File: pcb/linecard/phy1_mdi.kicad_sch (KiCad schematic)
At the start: 99 parts, among them J5 LPJG47036AWNL, J9 LPJG47036AWNL, U35 VSC8512, U36 ESD224DQAR, U37 ESD224DQAR, U38 ESD224DQAR, U39 ESD224DQAR, U40 ESD224DQAR, U41 ESD224DQAR, U42 ESD224DQAR, U43 ESD224DQAR, U44 ESD224DQAR, U45 ESD224DQAR, U46 ESD224DQAR, U47 ESD224DQAR, U48 ESD224DQAR, U49 ESD224DQAR, U50 ESD224DQAR, U51 ESD224DQAR, U52 ESD224DQAR, U53 ESD224DQAR, U54 ESD224DQAR, U55 ESD224DQAR, U56 ESD224DQAR, U57 ESD224DQAR, U58 ESD224DQAR, U59 ESD224DQAR

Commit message: Finished initial schematic review
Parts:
- J5, J9: footprint (none) -> azonenberg_pcb:CONN_LINKPP_LPJG47036AWNL
- U36, U37, U38, U39, U40, U41, U42, U43, U44, U45, U46, U47, U48, U49, U50, U51, U52, U53, U54, U55, U56, U57, U58, U59: footprint (none) -> azonenberg_pcb:DFN_10_0.5MM_2.5x1MM_TI_DQA
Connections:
- net CHGND: now also J9.SHLD, J9.SHLD, J9.SHLD, J9.SHLD, J9.SHLD, J9.SHLD, J9.SHLD, J9.SHLD; no longer J9.A0 (SHLD), J9.B0 (SHLD), J9.C0 (SHLD), J9.D0 (SHLD), J9.E0 (SHLD), J9.F0 (SHLD), J9.G0 (SHLD), J9.H0 (SHLD)
- net PHY0_D1_P: now also U36.6 (IO4_S); no longer U36.5 (IO4_S)
- net PHY0_D3_P: now also U37.6 (IO4_S); no longer U37.5 (IO4_S)
- net PHY10_D1_P: now also U56.6 (IO4_S); no longer U56.5 (IO4_S)
- net PHY10_D3_P: now also U57.6 (IO4_S); no longer U57.5 (IO4_S)
- net PHY11_D1_P: now also U58.6 (IO4_S); no longer U58.5 (IO4_S)
- net PHY11_D3_P: now also U59.6 (IO4_S); no longer U59.5 (IO4_S)
- net PHY1_D1_P: now also U38.6 (IO4_S); no longer U38.5 (IO4_S)
- net PHY1_D3_P: now also U39.6 (IO4_S); no longer U39.5 (IO4_S)
- net PHY2_D1_P: now also U40.6 (IO4_S); no longer U40.5 (IO4_S)
- net PHY2_D3_P: now also U41.6 (IO4_S); no longer U41.5 (IO4_S)
- net PHY3_D1_P: now also U42.6 (IO4_S); no longer U42.5 (IO4_S)
- net PHY3_D3_P: now also U43.6 (IO4_S); no longer U43.5 (IO4_S)
- net PHY4_D1_P: now also U44.6 (IO4_S); no longer U44.5 (IO4_S)
- net PHY4_D3_P: now also U45.6 (IO4_S); no longer U45.5 (IO4_S)
- net PHY5_D1_P: now also U46.6 (IO4_S); no longer U46.5 (IO4_S)
- net PHY5_D3_P: now also U47.6 (IO4_S); no longer U47.5 (IO4_S)
- net PHY6_D1_P: now also U48.6 (IO4_S); no longer U48.5 (IO4_S)
- net PHY6_D3_P: now also U49.6 (IO4_S); no longer U49.5 (IO4_S)
- net PHY7_D1_P: now also U50.6 (IO4_S); no longer U50.5 (IO4_S)
- net PHY7_D3_P: now also U51.6 (IO4_S); no longer U51.5 (IO4_S)
- net PHY8_D1_P: now also U52.6 (IO4_S); no longer U52.5 (IO4_S)
- net PHY8_D3_P: now also U53.6 (IO4_S); no longer U53.5 (IO4_S)
- net PHY9_D1_P: now also U54.6 (IO4_S); no longer U54.5 (IO4_S)
- net PHY9_D3_P: now also U55.6 (IO4_S); no longer U55.5 (IO4_S)

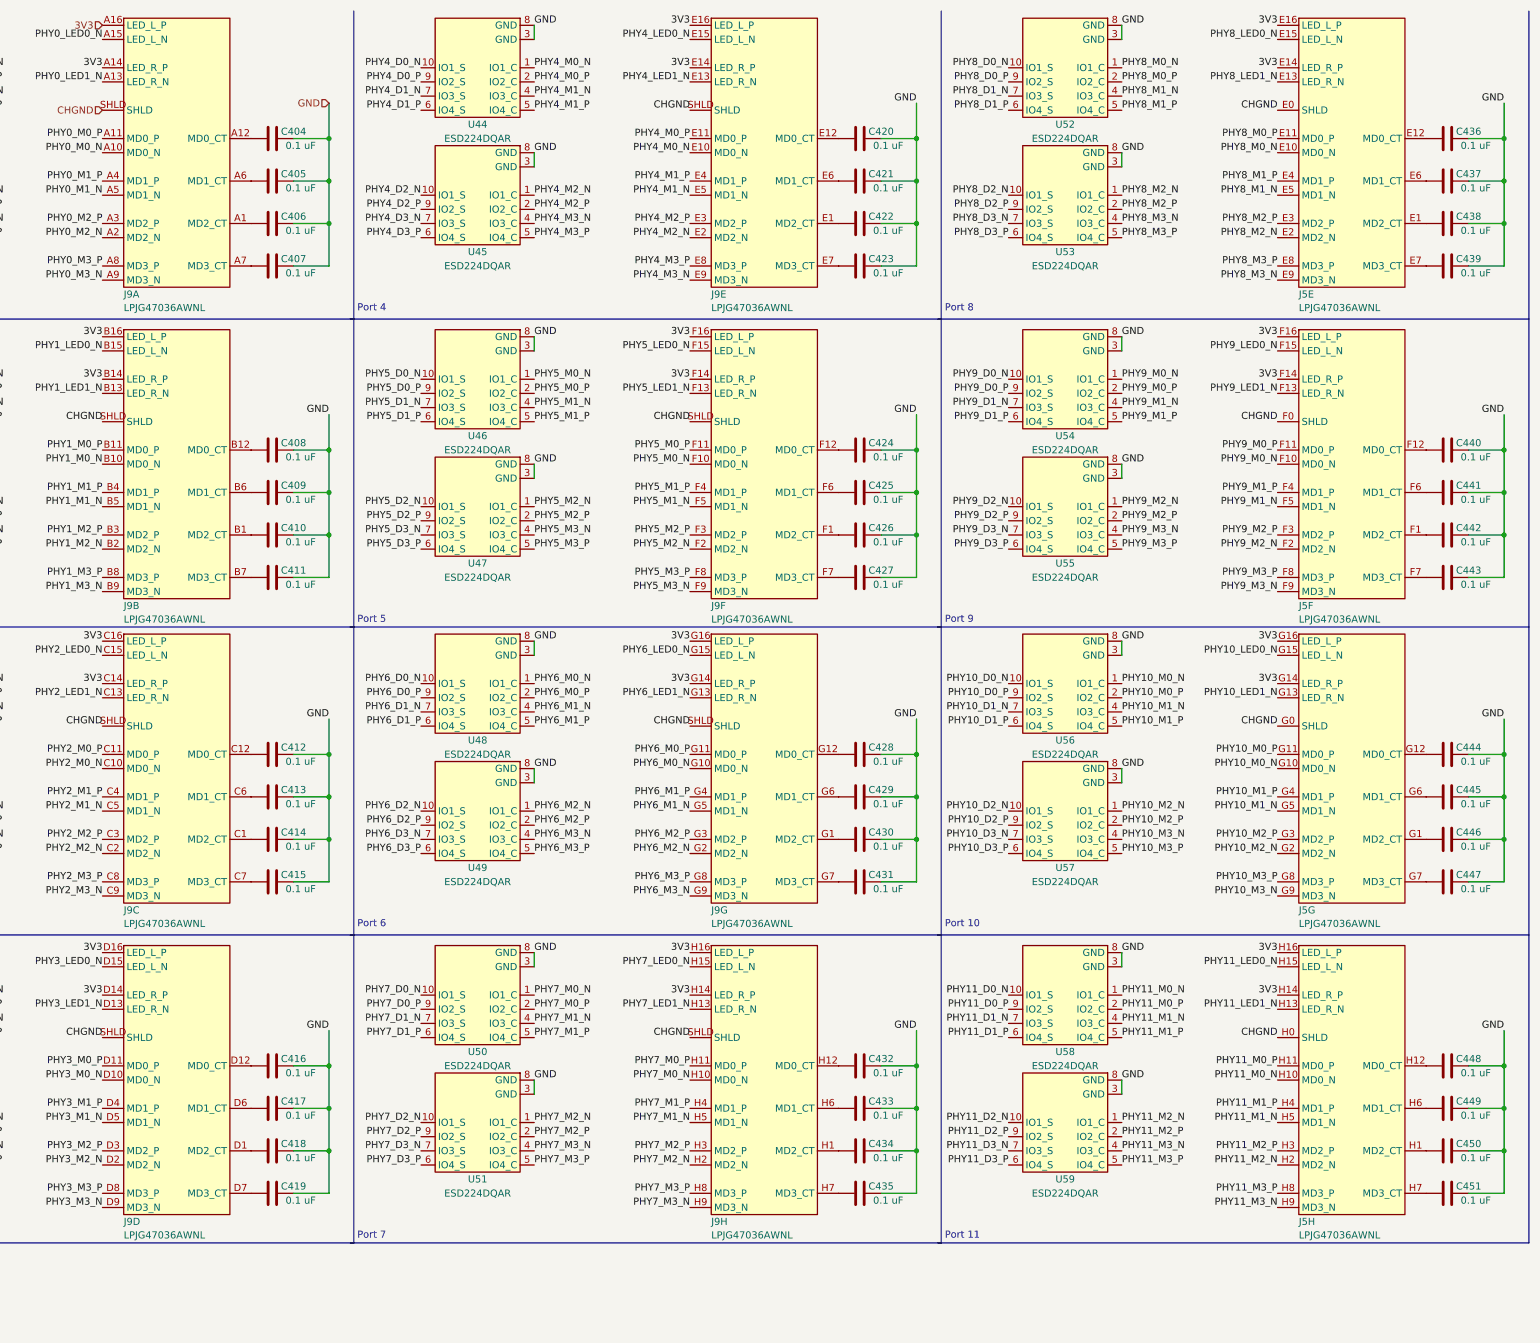
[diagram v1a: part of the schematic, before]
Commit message: COntinued routing baseT pairs on left PHY
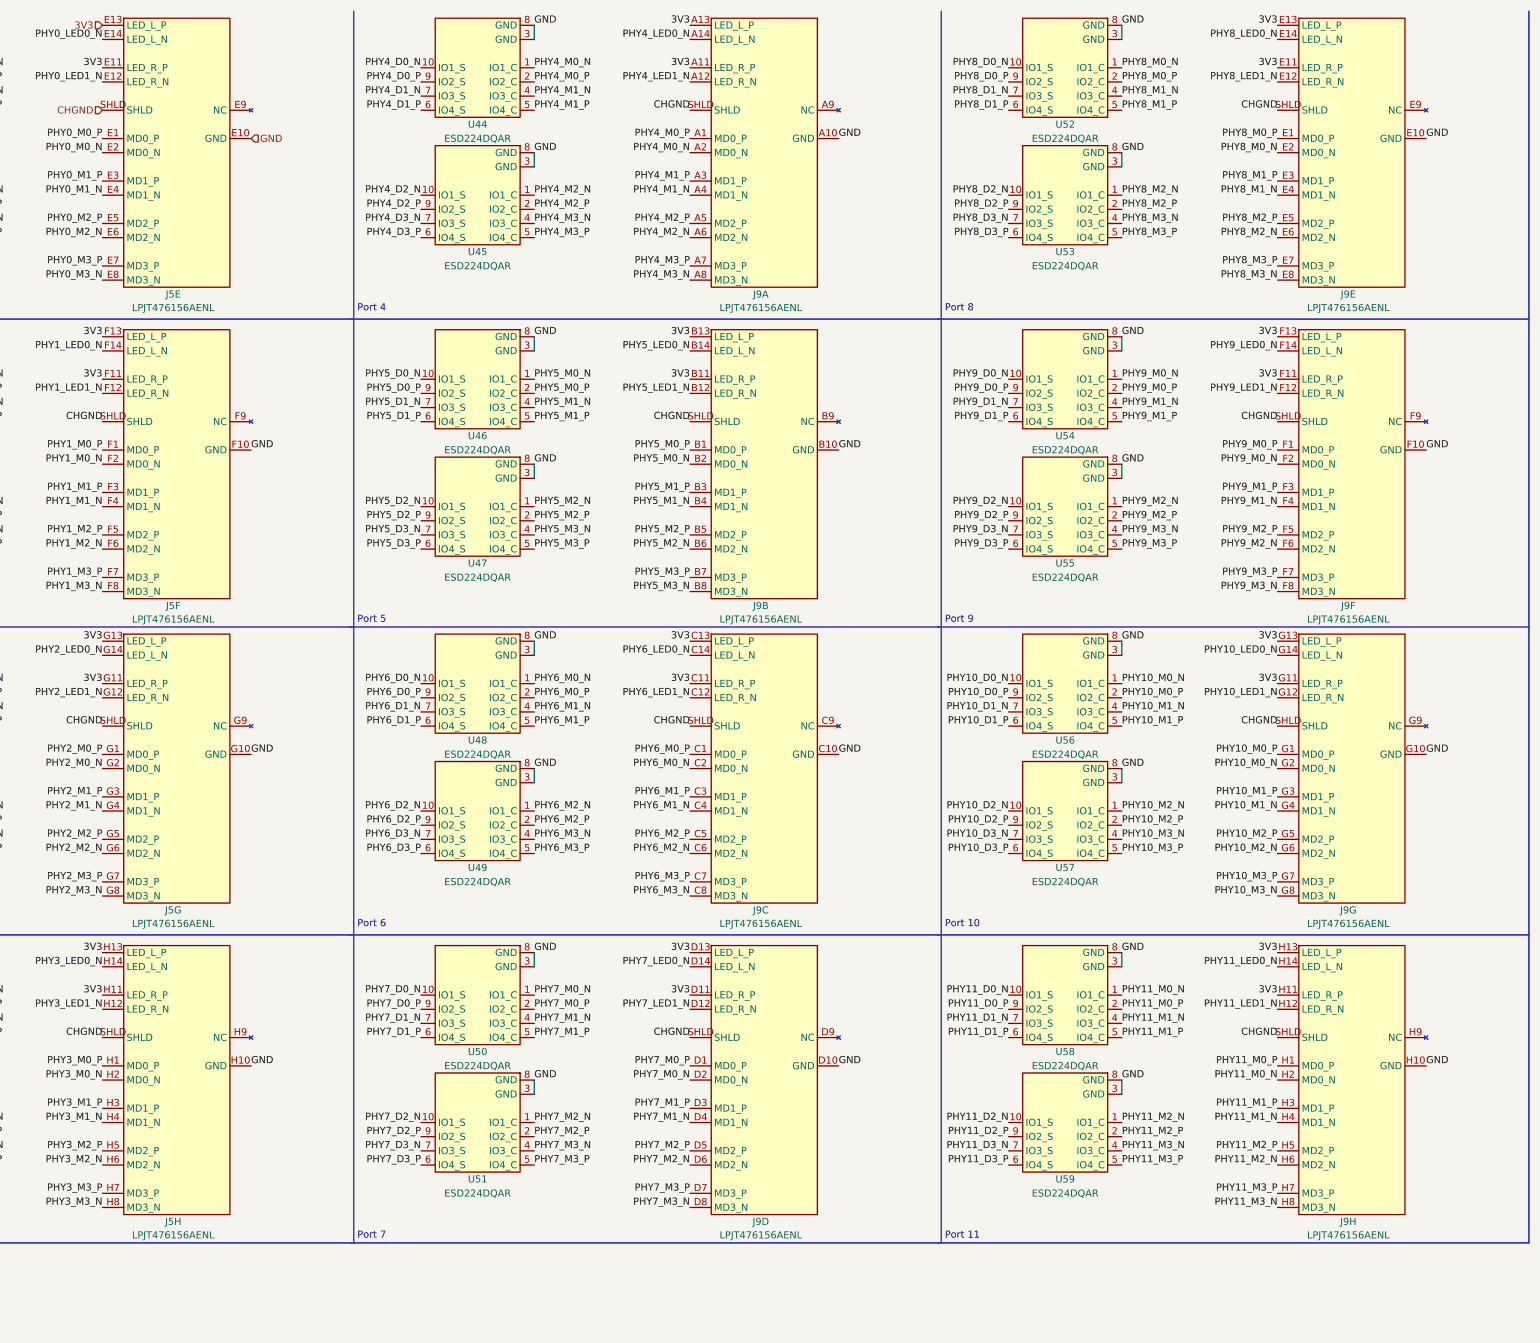
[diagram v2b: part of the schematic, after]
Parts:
- removed C404, C405, C406, C407, C408, C409, C410, C411, C412, C413, C414, C415, C416, C417, C418, C419, C420, C421, C422, C423, C424, C425, C426, C427, C428, C429, C430, C431, C432, C433, C434, C435, C436, C437, C438, C439, C440, C441, C442, C443, C444, C445, C446, C447, C448, C449, C450, C451: 0.1 uF, azonenberg_pcb:EIA_0402_CAP_NOSILK, symbol device:C
- removed J5, J9: LPJG47036AWNL, azonenberg_pcb:CONN_LINKPP_LPJG47036AWNL, symbol special-azonenberg:LPJG47036AWNL
- added J5, J9: LPJT476156AENL, azonenberg_pcb:CONN_LINKPP_LPJT476156AENL, symbol special-azonenberg:LPJT476156AENL
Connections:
- net 3V3: now also J5.E11 (LED_R_P), J5.E13 (LED_L_P), J5.F11 (LED_R_P), J5.F13 (LED_L_P), J5.G11 (LED_R_P), J5.G13 (LED_L_P), J5.H11 (LED_R_P), J5.H13 (LED_L_P), J9.A11 (LED_R_P), J9.A13 (LED_L_P), J9.B11 (LED_R_P), J9.B13 (LED_L_P), J9.C11 (LED_R_P), J9.C13 (LED_L_P), J9.D11 (LED_R_P), J9.D13 (LED_L_P), J9.E11 (LED_R_P), J9.E13 (LED_L_P), J9.F11 (LED_R_P), J9.F13 (LED_L_P), J9.G11 (LED_R_P), J9.G13 (LED_L_P), J9.H11 (LED_R_P), J9.H13 (LED_L_P)
- net CHGND: now also J5.SHLD, J5.SHLD, J5.SHLD, J5.SHLD, J9.SHLD, J9.SHLD, J9.SHLD, J9.SHLD, J9.SHLD, J9.SHLD, J9.SHLD, J9.SHLD
- net GND: now also J5.E10 (GND), J5.F10 (GND), J5.G10 (GND), J5.H10 (GND), J9.A10 (GND), J9.B10 (GND), J9.C10 (GND), J9.D10 (GND), J9.E10 (GND), J9.F10 (GND), J9.G10 (GND), J9.H10 (GND)
- net PHY0_LED0_N: now also J5.E14 (LED_L_N)
- net PHY0_LED1_N: now also J5.E12 (LED_R_N)
- net PHY0_M0_N: now also J5.E2 (MD0_N)
- net PHY0_M0_P: now also J5.E1 (MD0_P)
- net PHY0_M1_N: now also J5.E4 (MD1_N)
- net PHY0_M1_P: now also J5.E3 (MD1_P)
- net PHY0_M2_N: now also J5.E6 (MD2_N)
- net PHY0_M2_P: now also J5.E5 (MD2_P)
- net PHY0_M3_N: now also J5.E8 (MD3_N)
- net PHY0_M3_P: now also J5.E7 (MD3_P)
- net PHY10_LED0_N: now also J9.G14 (LED_L_N)
- net PHY10_LED1_N: now also J9.G12 (LED_R_N)
- net PHY10_M0_N: now also J9.G2 (MD0_N)
- net PHY10_M0_P: now also J9.G1 (MD0_P)
- net PHY10_M1_N: now also J9.G4 (MD1_N)
- net PHY10_M1_P: now also J9.G3 (MD1_P)
- net PHY10_M2_N: now also J9.G6 (MD2_N)
- net PHY10_M2_P: now also J9.G5 (MD2_P)
- net PHY10_M3_N: now also J9.G8 (MD3_N)
- net PHY10_M3_P: now also J9.G7 (MD3_P)
- net PHY11_LED0_N: now also J9.H14 (LED_L_N)
- net PHY11_LED1_N: now also J9.H12 (LED_R_N)
- net PHY11_M0_N: now also J9.H2 (MD0_N)
- net PHY11_M0_P: now also J9.H1 (MD0_P)
- net PHY11_M1_N: now also J9.H4 (MD1_N)
- net PHY11_M1_P: now also J9.H3 (MD1_P)
- net PHY11_M2_N: now also J9.H6 (MD2_N)
- net PHY11_M2_P: now also J9.H5 (MD2_P)
- net PHY11_M3_N: now also J9.H8 (MD3_N)
- net PHY11_M3_P: now also J9.H7 (MD3_P)
- net PHY1_LED0_N: now also J5.F14 (LED_L_N)
- net PHY1_LED1_N: now also J5.F12 (LED_R_N)
- net PHY1_M0_N: now also J5.F2 (MD0_N)
- net PHY1_M0_P: now also J5.F1 (MD0_P)
- net PHY1_M1_N: now also J5.F4 (MD1_N)
- net PHY1_M1_P: now also J5.F3 (MD1_P)
- net PHY1_M2_N: now also J5.F6 (MD2_N)
- net PHY1_M2_P: now also J5.F5 (MD2_P)
- net PHY1_M3_N: now also J5.F8 (MD3_N)
- net PHY1_M3_P: now also J5.F7 (MD3_P)
- net PHY2_LED0_N: now also J5.G14 (LED_L_N)
- net PHY2_LED1_N: now also J5.G12 (LED_R_N)
- net PHY2_M0_N: now also J5.G2 (MD0_N)
- net PHY2_M0_P: now also J5.G1 (MD0_P)
- net PHY2_M1_N: now also J5.G4 (MD1_N)
- net PHY2_M1_P: now also J5.G3 (MD1_P)
- net PHY2_M2_N: now also J5.G6 (MD2_N)
- net PHY2_M2_P: now also J5.G5 (MD2_P)
- net PHY2_M3_N: now also J5.G8 (MD3_N)
- net PHY2_M3_P: now also J5.G7 (MD3_P)
- net PHY3_LED0_N: now also J5.H14 (LED_L_N)
- net PHY3_LED1_N: now also J5.H12 (LED_R_N)
- net PHY3_M0_N: now also J5.H2 (MD0_N)
- net PHY3_M0_P: now also J5.H1 (MD0_P)
- net PHY3_M1_N: now also J5.H4 (MD1_N)
- net PHY3_M1_P: now also J5.H3 (MD1_P)
- net PHY3_M2_N: now also J5.H6 (MD2_N)
- net PHY3_M2_P: now also J5.H5 (MD2_P)
- net PHY3_M3_N: now also J5.H8 (MD3_N)
- net PHY3_M3_P: now also J5.H7 (MD3_P)
- net PHY4_LED0_N: now also J9.A14 (LED_L_N)
- net PHY4_LED1_N: now also J9.A12 (LED_R_N)
- net PHY4_M0_N: now also J9.A2 (MD0_N)
- net PHY4_M0_P: now also J9.A1 (MD0_P)
- net PHY4_M1_N: now also J9.A4 (MD1_N)
- net PHY4_M1_P: now also J9.A3 (MD1_P)
- net PHY4_M2_N: now also J9.A6 (MD2_N)
- net PHY4_M2_P: now also J9.A5 (MD2_P)
- net PHY4_M3_N: now also J9.A8 (MD3_N)
- net PHY4_M3_P: now also J9.A7 (MD3_P)
- net PHY5_LED0_N: now also J9.B14 (LED_L_N)
- net PHY5_LED1_N: now also J9.B12 (LED_R_N)
- net PHY5_M0_N: now also J9.B2 (MD0_N)
- net PHY5_M0_P: now also J9.B1 (MD0_P)
- net PHY5_M1_N: now also J9.B4 (MD1_N)
- net PHY5_M1_P: now also J9.B3 (MD1_P)
- net PHY5_M2_N: now also J9.B6 (MD2_N)
- net PHY5_M2_P: now also J9.B5 (MD2_P)
- net PHY5_M3_N: now also J9.B8 (MD3_N)
- net PHY5_M3_P: now also J9.B7 (MD3_P)
- net PHY6_LED0_N: now also J9.C14 (LED_L_N)
- net PHY6_LED1_N: now also J9.C12 (LED_R_N)
- net PHY6_M0_N: now also J9.C2 (MD0_N)
- net PHY6_M0_P: now also J9.C1 (MD0_P)
- net PHY6_M1_N: now also J9.C4 (MD1_N)
- net PHY6_M1_P: now also J9.C3 (MD1_P)
- net PHY6_M2_N: now also J9.C6 (MD2_N)
- net PHY6_M2_P: now also J9.C5 (MD2_P)
- net PHY6_M3_N: now also J9.C8 (MD3_N)
- net PHY6_M3_P: now also J9.C7 (MD3_P)
- net PHY7_LED0_N: now also J9.D14 (LED_L_N)
- net PHY7_LED1_N: now also J9.D12 (LED_R_N)
- net PHY7_M0_N: now also J9.D2 (MD0_N)
- net PHY7_M0_P: now also J9.D1 (MD0_P)
- net PHY7_M1_N: now also J9.D4 (MD1_N)
- net PHY7_M1_P: now also J9.D3 (MD1_P)
- net PHY7_M2_N: now also J9.D6 (MD2_N)
- net PHY7_M2_P: now also J9.D5 (MD2_P)
- net PHY7_M3_N: now also J9.D8 (MD3_N)
- net PHY7_M3_P: now also J9.D7 (MD3_P)
- net PHY8_LED0_N: now also J9.E14 (LED_L_N)
- net PHY8_LED1_N: now also J9.E12 (LED_R_N)
- net PHY8_M0_N: now also J9.E2 (MD0_N)
- net PHY8_M0_P: now also J9.E1 (MD0_P)
- net PHY8_M1_N: now also J9.E4 (MD1_N)
- net PHY8_M1_P: now also J9.E3 (MD1_P)
- net PHY8_M2_N: now also J9.E6 (MD2_N)
- net PHY8_M2_P: now also J9.E5 (MD2_P)
- net PHY8_M3_N: now also J9.E8 (MD3_N)
- net PHY8_M3_P: now also J9.E7 (MD3_P)
- net PHY9_LED0_N: now also J9.F14 (LED_L_N)
- net PHY9_LED1_N: now also J9.F12 (LED_R_N)
- net PHY9_M0_N: now also J9.F2 (MD0_N)
- net PHY9_M0_P: now also J9.F1 (MD0_P)
- net PHY9_M1_N: now also J9.F4 (MD1_N)
- net PHY9_M1_P: now also J9.F3 (MD1_P)
- net PHY9_M2_N: now also J9.F6 (MD2_N)
- net PHY9_M2_P: now also J9.F5 (MD2_P)
- net PHY9_M3_N: now also J9.F8 (MD3_N)
- net PHY9_M3_P: now also J9.F7 (MD3_P)
